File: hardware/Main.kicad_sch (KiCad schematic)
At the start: 23 parts, among them IC102 APDS-9306-065, IC103 BME688, M101 BL54L15, Q101 BSS84, SW101 JOIN, X102 DEBUG

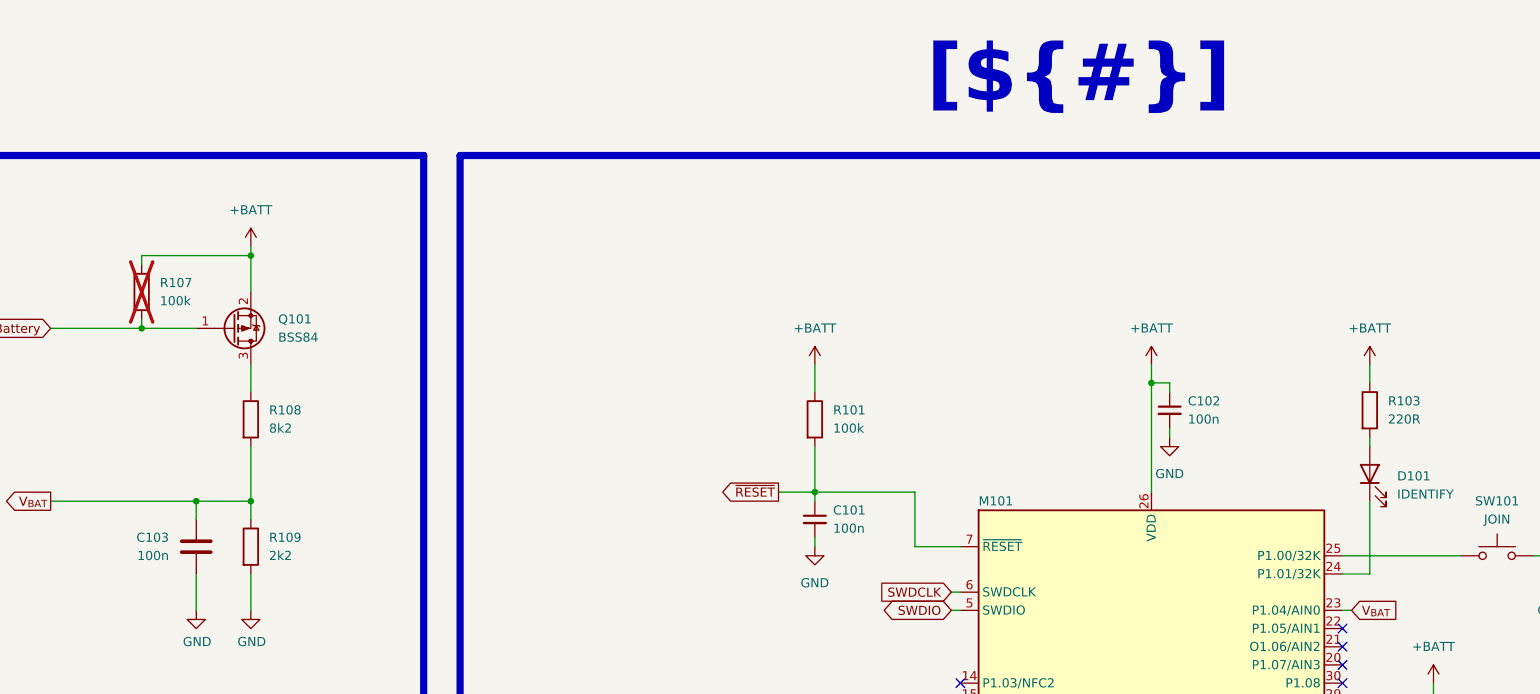
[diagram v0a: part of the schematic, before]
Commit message: - Change ADC filter capacitor to 1 nF - Update documentation with current consumption - Update CI/CD pipeline
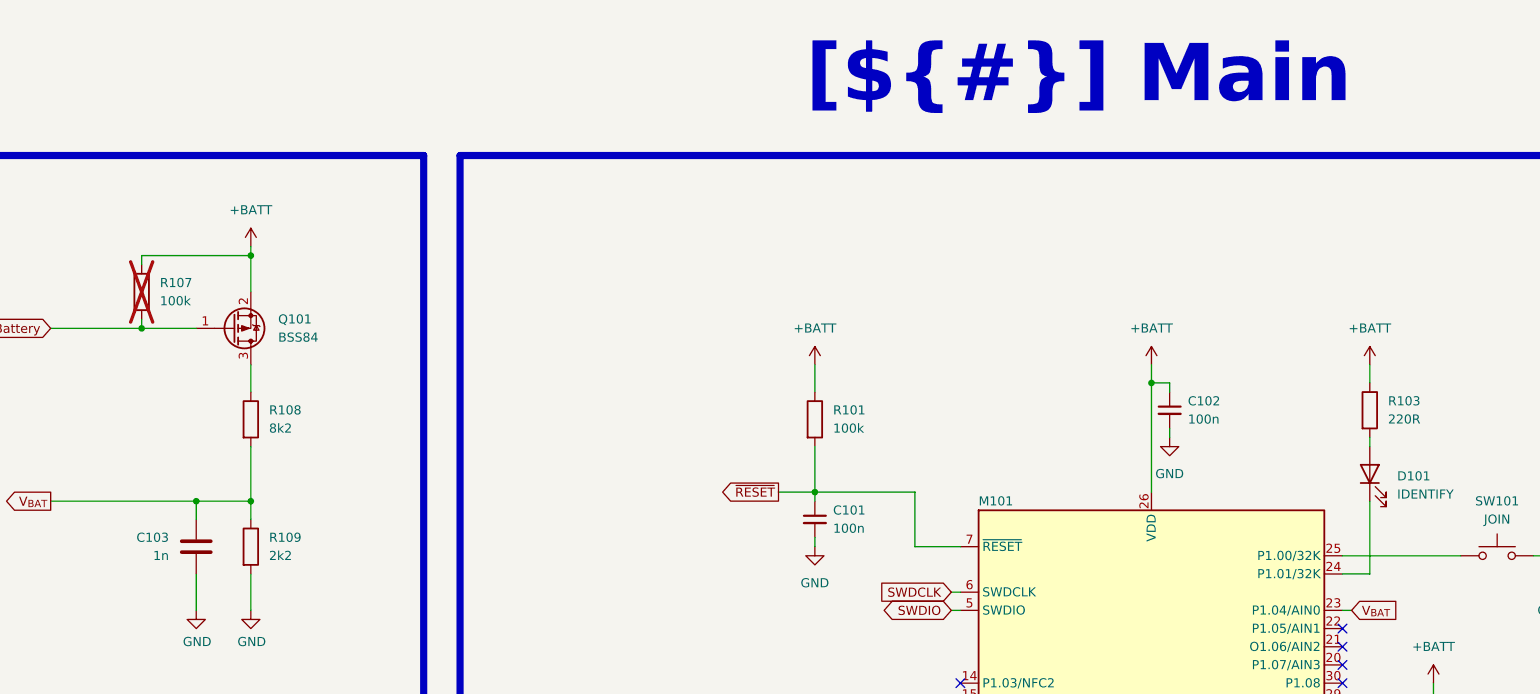
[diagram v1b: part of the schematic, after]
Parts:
- C103: value 100n -> 1n; manf KYOCERA AVX -> Murata Electronics; manf# 04025C104KAT4A -> GCM1555C2A102JE02D; mouser# 581-04025C104KAT4A -> 81-GCM1555C2A102JE02D
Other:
- title: (none) -> Main
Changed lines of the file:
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@@
 	(paper "A3")
 	(title_block
+		(title "Main")
 		(date "2025-06-05")
 		(rev "${REVISION}")
@@
 			)
 		)
-		(property "Value" "100n"
+		(property "Value" "1n"
 			(at 82.55 93.98 0)
 			(effects
@@
 			)
 		)
-		(property "Datasheet" "https://www.mouser.de/datasheet/2/40/KGM_X7R-3223212.pdf"
+		(property "Datasheet" "https://search.murata.co.jp/Ceramy/image/img/A01X/G101/ENG/GCM1555C2A102JE02-01A.pdf"
 			(at 86.36 92.71 0)
 			(effects
@@
 			)
 		)
-		(property "manf" "KYOCERA AVX"
+		(property "manf" "Murata Electronics"
 			(at 86.36 92.71 0)
 			(effects
@@
 			)
 		)
-		(property "manf#" "04025C104KAT4A"
+		(property "manf#" "GCM1555C2A102JE02D"
 			(at 86.36 92.71 0)
 			(effects
@@
 			)
 		)
-		(property "mouser#" "581-04025C104KAT4A"
+		(property "mouser#" "81-GCM1555C2A102JE02D"
+			(at 86.36 92.71 0)
+			(effects
+				(font
+					(size 1.27 1.27)
+				)
+				(hide yes)
+			)
+		)
+		(property "CONFIG" ""
 			(at 86.36 92.71 0)
 			(effects
